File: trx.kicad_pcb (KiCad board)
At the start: 2 copper layers, 100.3 x 63.5 mm, 99 parts, among them J1 12V, J2 HF, J3 Volume, J4 Conn_01x04, J5 HP, J6 OSC-I, J7 OSC-Q, J8 TX, J9 12V, Q1 BS170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

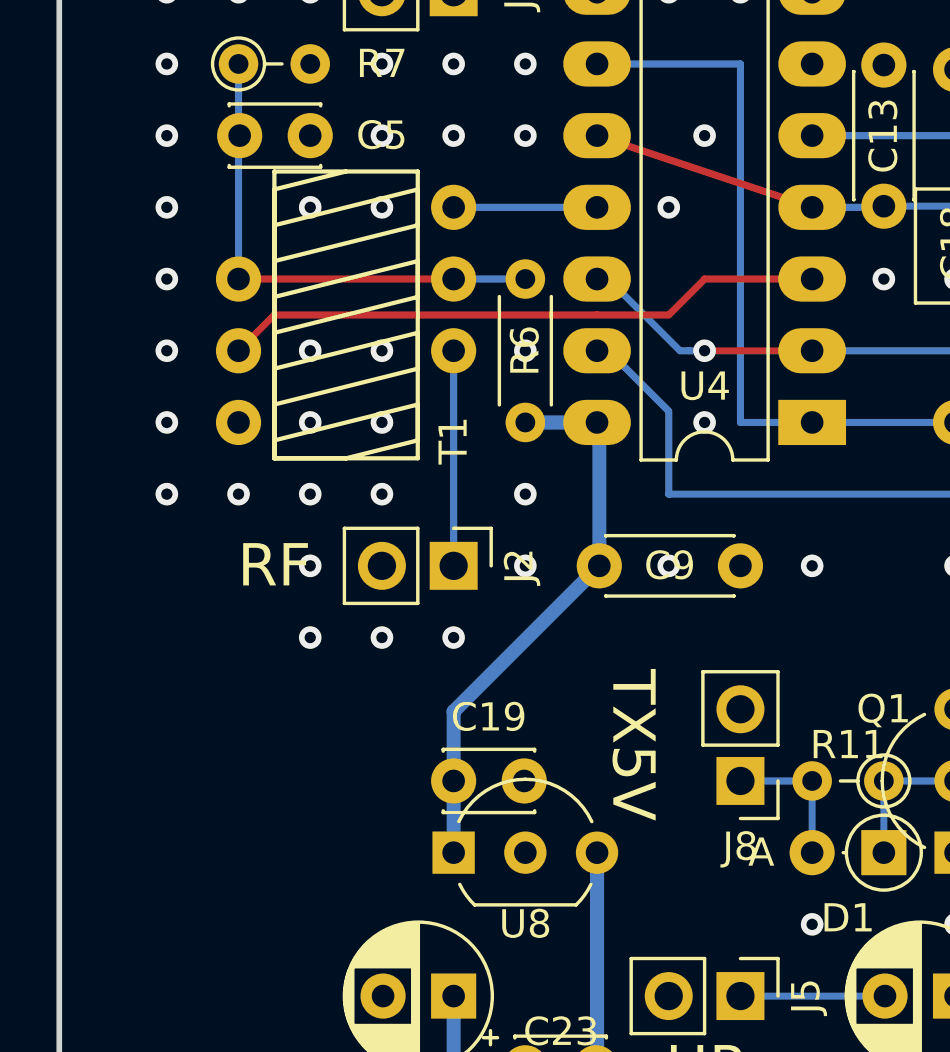
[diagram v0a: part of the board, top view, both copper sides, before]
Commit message: Added libs and fixed footprints.
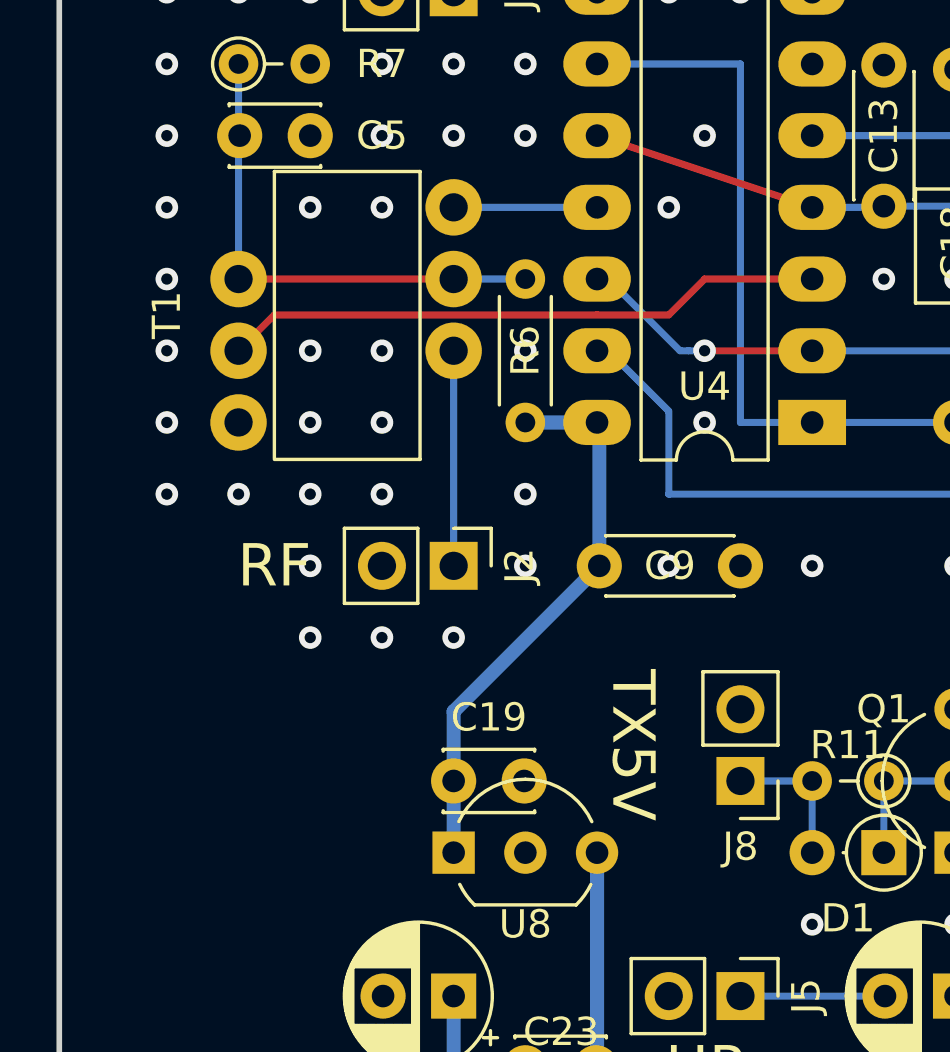
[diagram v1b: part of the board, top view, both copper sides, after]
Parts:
- R9: value 33k -> 3,3k
- T1: footprint Transformer_THT:Transformer_Toroid_Tapped_Vertical_D10.5mm_Amidon-T37 -> DM3MAT:Transformer_1P_2S_Toroid_Vertical_D10.5mm_Amidon-T37_Wide
- U1, U2, U3, U6, U7: value TL072 -> LM833
- U5: value TL072 -> TLC272
- moved T1 4.02 mm to (105.4, 81.3), turned to 90 degrees
